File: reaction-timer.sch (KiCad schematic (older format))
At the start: 35 parts, among them IC1 4026, IC2 4026, IC3 4026, IC5 NE555P, IC6 NE555P, IC7 NE555P

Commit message: Change button footprints to pin header instead of wire pad
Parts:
- S2, S3, S4: footprint Wire_Pads:SolderWirePad_2x_1mmDrill -> Pin_Headers:Pin_Header_Straight_1x02
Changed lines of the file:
@@
 F 0 "S4" H 3550 1410 50  0000 C CNN
 F 1 "START_DELAY" H 3400 1220 50  0000 C CNN
-F 2 "Wire_Pads:SolderWirePad_2x_1mmDrill" H 3400 1300 60  0001 C CNN
+F 2 "Pin_Headers:Pin_Header_Straight_1x02" H 3400 1300 60  0001 C CNN
 F 3 "" H 3400 1300 60  0000 C CNN
 	1    3400 1300
@@
 F 0 "S3" H 3250 3410 50  0000 C CNN
 F 1 "STOP" H 3100 3220 50  0000 C CNN
-F 2 "Wire_Pads:SolderWirePad_2x_1mmDrill" H 3100 3300 60  0001 C CNN
+F 2 "Pin_Headers:Pin_Header_Straight_1x02" H 3100 3300 60  0001 C CNN
 F 3 "" H 3100 3300 60  0000 C CNN
 	1    3100 3300
@@
 F 0 "S2" H 5550 5410 50  0000 C CNN
 F 1 "SET_TO_ZERO" H 5400 5220 50  0000 C CNN
-F 2 "Wire_Pads:SolderWirePad_2x_1mmDrill" H 5400 5300 60  0001 C CNN
+F 2 "Pin_Headers:Pin_Header_Straight_1x02" H 5400 5300 60  0001 C CNN
 F 3 "" H 5400 5300 60  0000 C CNN
 	1    5400 5300

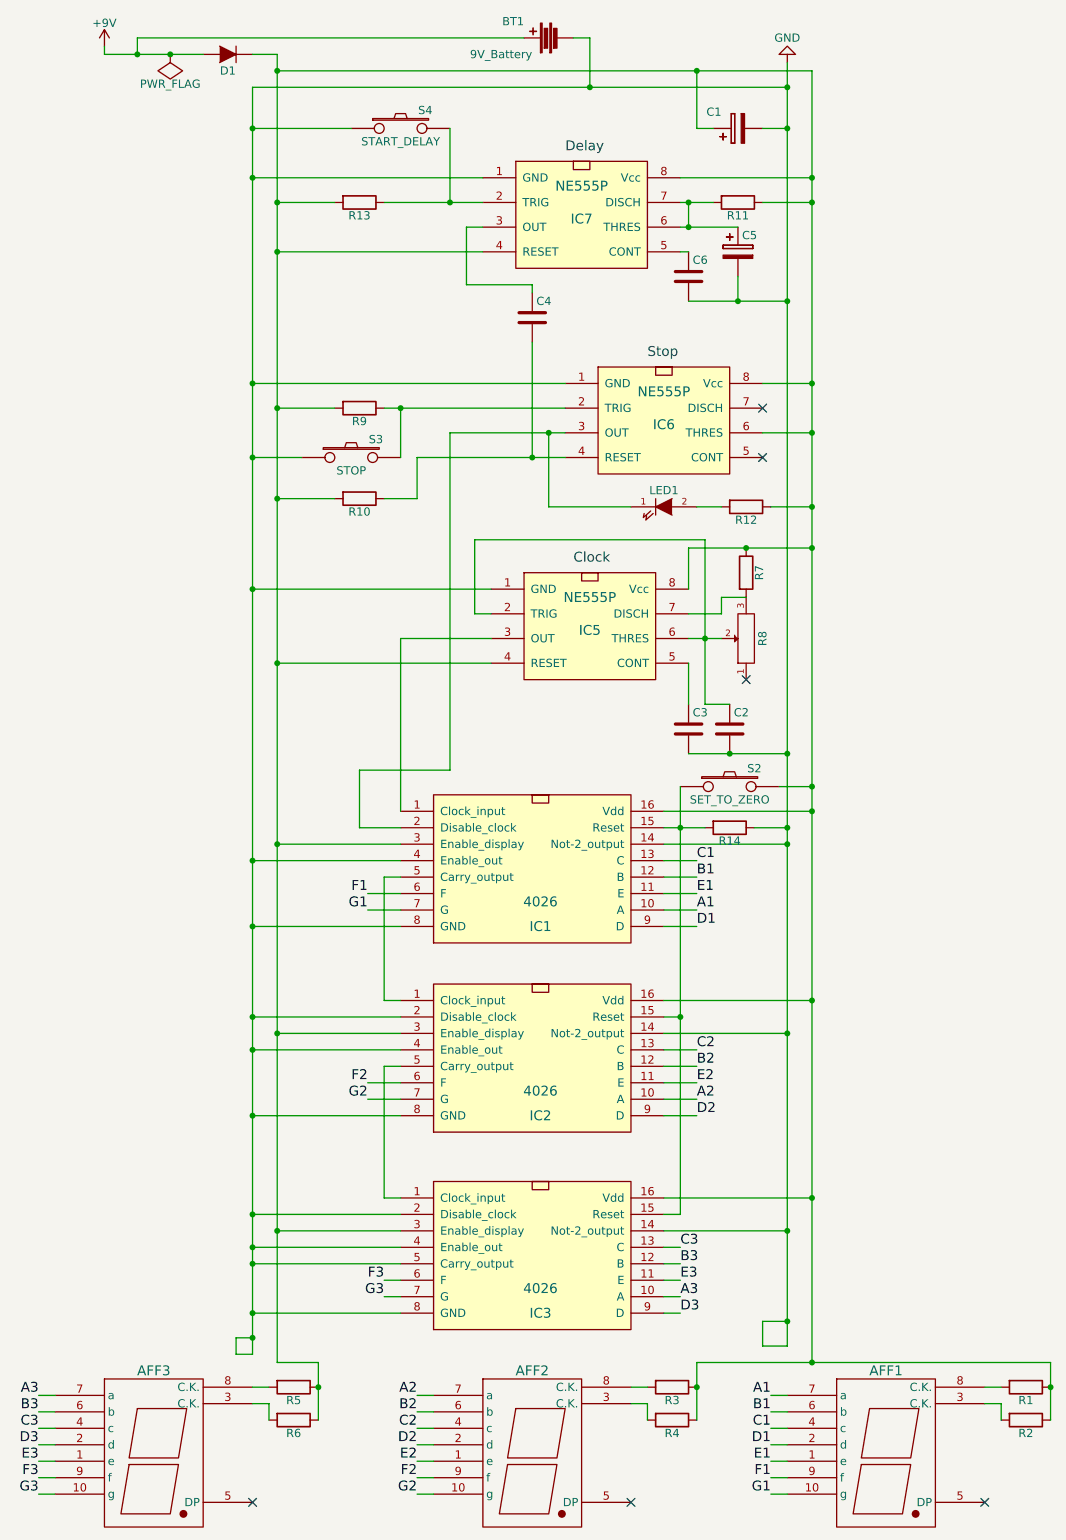
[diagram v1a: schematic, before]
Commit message: Fix 7-seg common anode/cathode schematic confusion
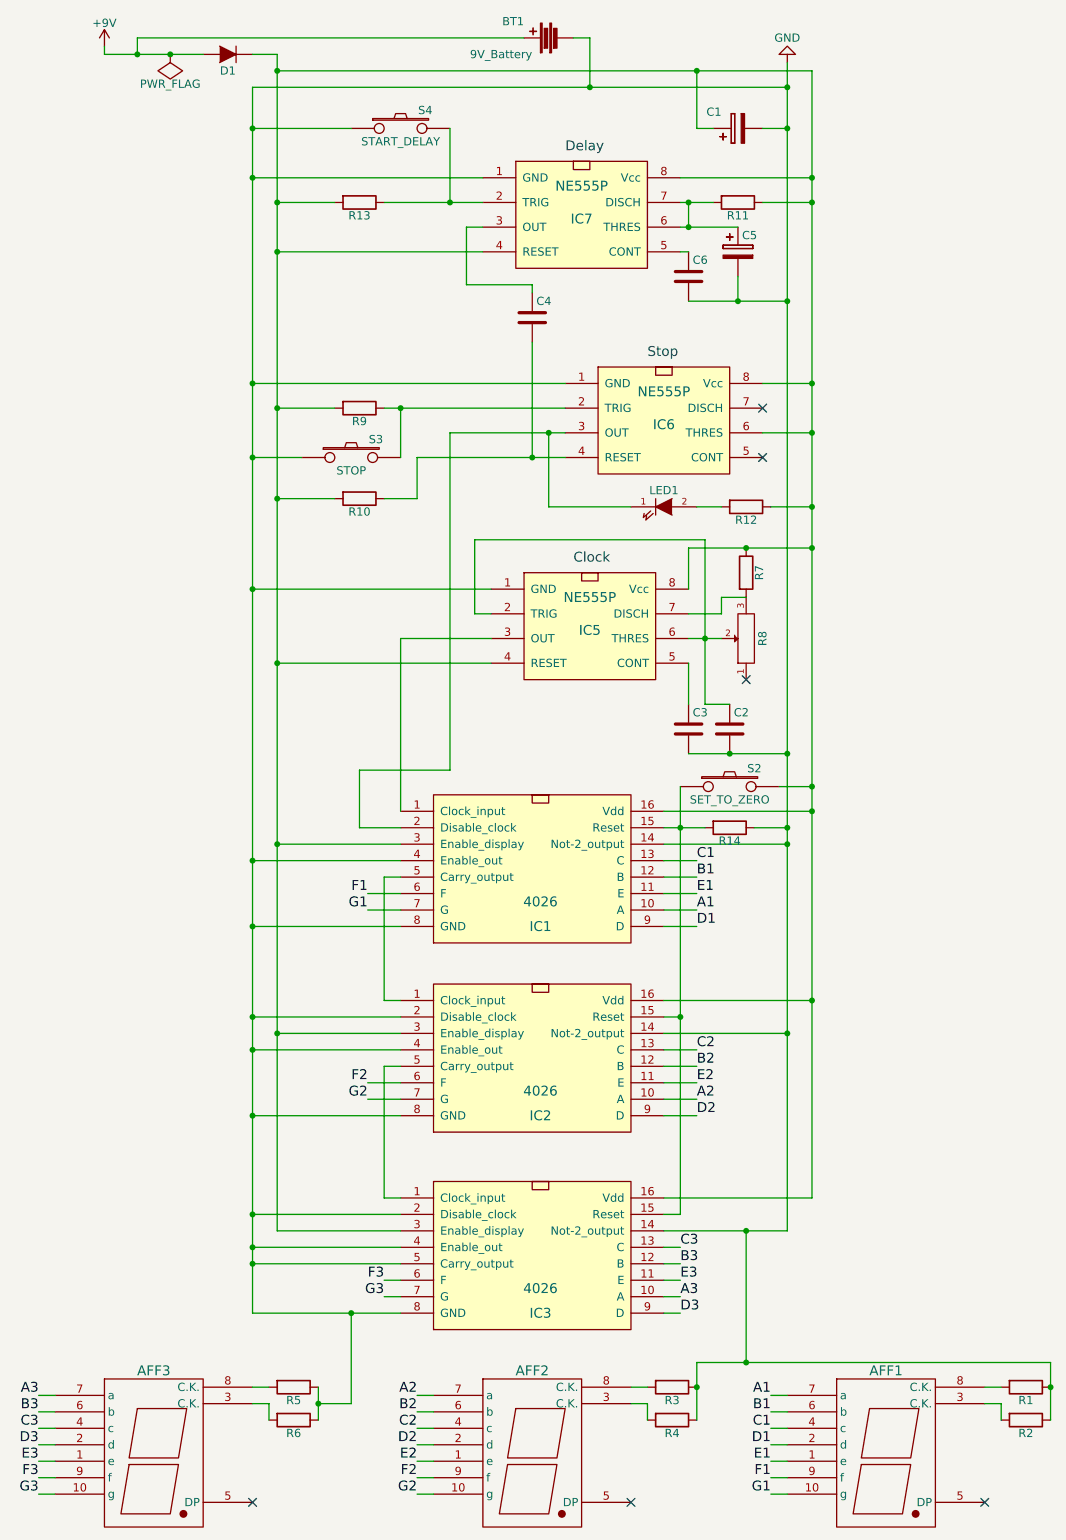
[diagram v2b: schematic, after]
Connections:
- net GND: now also R1.1, R2.1, R3.1, R4.1, R5.1, R6.1
- net at C1.1, D1.1 (K), IC1.16 (Vdd)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: no longer R1.1, R2.1, R3.1, R4.1, R5.1, R6.1

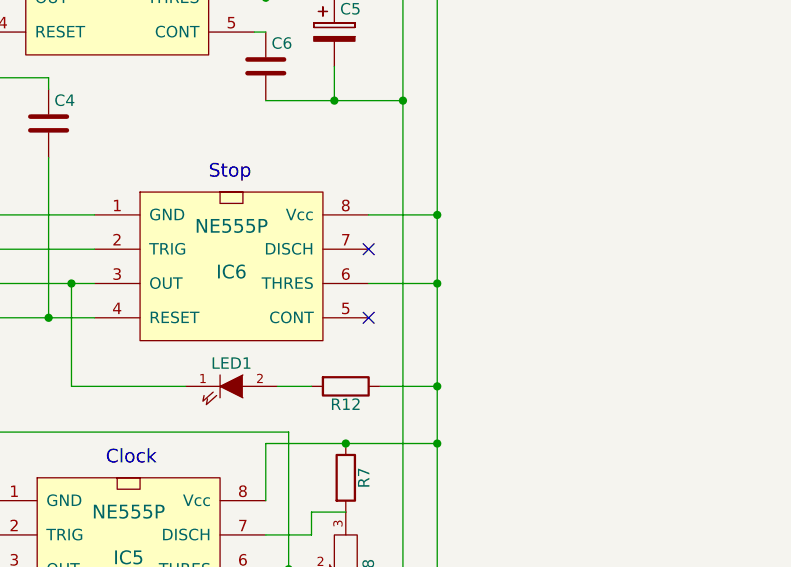
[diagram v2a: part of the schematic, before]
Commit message: Bugfix: IC6 pin 6 should be GND not VCC
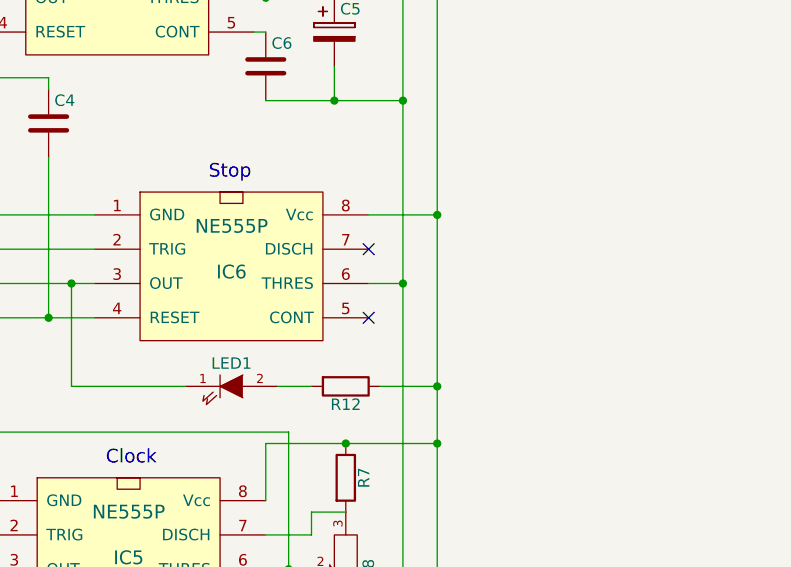
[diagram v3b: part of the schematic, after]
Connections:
- net GND: now also IC6.6 (THRES)
- net at C1.1, D1.1 (K), IC1.16 (Vdd)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: no longer IC6.6 (THRES)
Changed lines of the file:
@@
 Title "Reaction Timer"
 Date ""
-Rev "0.1.0"
+Rev "0.1.1"
 Comp "Simon Lundmark"
 Comment1 ""
@@
 Connection ~ 5900 2850
 Wire Wire Line
-	5900 3150 5600 3150
-Connection ~ 5900 3150
-Wire Wire Line
 	4200 2600 4200 3300
 Wire Wire Line
@@
 Connection ~ 5500 8800
 Connection ~ 5500 8000
+Wire Wire Line
+	5600 3150 5750 3150
+Connection ~ 5750 3150
 $EndSCHEMATC
